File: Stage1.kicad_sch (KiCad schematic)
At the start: 21 parts, among them Q3 SQJQ480E, Q5 IRFR210PBF, U2 LM74800QDRRRQ1

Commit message: new layout
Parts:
- removed D8: 1N4002, Diode_THT:D_DO-41_SOD81_P10.16mm_Horizontal, symbol Diode:1N4002
- added D4: MRA4003T3G, Diode_SMD:D_SMA, symbol Diode:MRA4003T3G
- D6: footprint Diode_THT:D_DO-35_SOD27_P7.62mm_Horizontal -> Diode_SMD:D_SOD-123
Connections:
- net GNDS is gone; now on net GND1: C10.2 (-), C11.2 (-), C2.2 (-), C5.2 (-), C9.2 (-), D2.1 (A1), NT1.1
- net OUT: now also D4.2 (A); no longer C2.1 (+), C5.1 (+), Q3.5 (D), R5.1 (+), U2.12 (C)
- net VS: now also D4.1 (K)
- new net SYSOUT: C2.1 (+), C5.1 (+), Q3.5 (D), R5.1 (+), U2.12 (C)
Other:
- moved on the sheet: NT1
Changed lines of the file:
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@@
+	)
+	(junction
+		(at 99.06 88.9)
+		(diameter 0)
+		(color 0 0 0 0)
 	)
 	(junction
@@
 	)
 	(junction
+		(at 90.17 88.9)
+		(diameter 0)
+		(color 0 0 0 0)
+	)
+	(junction
 		(at 85.09 78.74)
 		(diameter 0)
@@
 	(wire
 		(pts
+			(xy 99.06 90.17) (xy 99.06 88.9)
+		)
+		(stroke
+			(width 0)
+			(type default)
+		)
+	)
+	(wire
+		(pts
 			(xy 132.08 82.55) (xy 132.08 81.28)
 		)
@@
 	(wire
 		(pts
-			(xy 96.52 88.9) (xy 104.14 88.9)
+			(xy 96.52 90.17) (xy 99.06 90.17)
 		)
 		(stroke
@@
 	(wire
 		(pts
+			(xy 90.17 88.9) (xy 99.06 88.9)
+		)
+		(stroke
+			(width 0)
+			(type default)
+		)
+	)
+	(wire
+		(pts
+			(xy 90.17 88.9) (xy 85.09 88.9)
+		)
+		(stroke
+			(width 0)
+			(type default)
+		)
+	)
+	(wire
+		(pts
 			(xy 137.16 118.11) (xy 139.7 118.11)
 		)
@@
 	(wire
 		(pts
+			(xy 99.06 88.9) (xy 104.14 88.9)
+		)
+		(stroke
+			(width 0)
+			(type default)
+		)
+	)
+	(wire
+		(pts
 			(xy 175.26 118.11) (xy 179.07 118.11)
 		)
@@
 	(wire
 		(pts
+			(xy 90.17 90.17) (xy 90.17 88.9)
+		)
+		(stroke
+			(width 0)
+			(type default)
+		)
+	)
+	(wire
+		(pts
 			(xy 146.05 72.39) (xy 146.05 73.66)
 		)
@@
 	(wire
 		(pts
-			(xy 91.44 88.9) (xy 85.09 88.9)
+			(xy 91.44 90.17) (xy 90.17 90.17)
 		)
 		(stroke
@@
 		)
 	)
-	(hierarchical_label "OUT"
+	(hierarchical_label "SYSOUT"
 		(shape output)
 		(at 220.98 62.23 0)
@@
 			)
 		)
-		(property "Footprint" "Diode_THT:D_DO-35_SOD27_P7.62mm_Horizontal"
+		(property "Footprint" "Diode_SMD:D_SOD-123"
 			(at 127.635 77.47 0)
 			(effects
@@
 	)
 	(symbol
-		(lib_id "Diode:1N4002")
-		(at 146.05 77.47 270)
-		(unit 1)
-		(exclude_from_sim no)
-		(in_bom yes)
-		(on_board yes)
-		(dnp no)
-		(fields_autoplaced yes)
-		(property "Reference" "D8"
-			(at 148.59 76.1999 90)
-			(effects
-				(font
-					(size 1.27 1.27)
-				)
-				(justify left)
-			)
-		)
-		(property "Value" "1N4002"
-			(at 148.59 78.7399 90)
-			(effects
-				(font
-					(size 1.27 1.27)
-				)
-				(justify left)
-			)
-		)
-		(property "Footprint" "Diode_THT:D_DO-41_SOD81_P10.16mm_Horizontal"
-			(at 141.605 77.47 0)
-			(effects
-				(font
-					(size 1.27 1.27)
-				)
-				(hide yes)
-			)
-		)
-		(property "Datasheet" "http://www.vishay.com/docs/88503/1n4001.pdf"
-			(at 146.05 77.47 0)
-			(effects
-				(font
-					(size 1.27 1.27)
-				)
-				(hide yes)
-			)
-		)
-		(property "Description" "100V 1A General Purpose Rectifier Diode, DO-41"
-			(at 146.05 77.47 0)
-			(effects
-				(font
-					(size 1.27 1.27)
-				)
-				(hide yes)
-			)
-		)
-		(property "Sim.Device" "D"
-			(at 146.05 77.47 0)
-			(effects
-				(font
-					(size 1.27 1.27)
-				)
-				(hide yes)
-			)
-		)
-		(property "Sim.Pins" "1=K 2=A"
-			(at 146.05 77.47 0)
-			(effects
-				(font
-					(size 1.27 1.27)
-				)
-				(hide yes)
-			)
-		)
-		(pin "2"
-		)
-		(pin "1"
-		)
-		(instances
-			(project "OverVoltageProtection"
-				(path "/3ab01156-4af1-4058-a55c-fa6294991d75/6c85ee69-59dc-40d3-b5ed-3a4bea6d00bc"
-					(reference "D8")
-					(unit 1)
-				)
-			)
-		)
-	)
-	(symbol
 		(lib_id "PCM_Elektuur:C")
 		(at 120.65 77.47 0)
@@
 	(symbol
 		(lib_id "Device:NetTie_2")
-		(at 93.98 88.9 0)
+		(at 93.98 90.17 0)
+		(mirror y)
 		(unit 1)
 		(exclude_from_sim no)
@@
 		(dnp no)
 		(property "Reference" "NT1"
-			(at 93.98 90.678 0)
+			(at 93.98 91.948 0)
 			(effects
 				(font
@@
 		)
 		(property "Value" "NetTie_2"
-			(at 93.98 93.218 0)
+			(at 93.98 94.488 0)
 			(effects
 				(font
@@
 		)
 		(property "Footprint" ""
-			(at 93.98 88.9 0)
+			(at 93.98 90.17 0)
 			(effects
 				(font
@@
 		)
 		(property "Datasheet" "~"
-			(at 93.98 88.9 0)
+			(at 93.98 90.17 0)
 			(effects
 				(font
@@
 		)
 		(property "Description" "Net tie, 2 pins"
-			(at 93.98 88.9 0)
+			(at 93.98 90.17 0)
 			(effects
 				(font
@@
 					(unit 1)
 				)
+			)
+		)
+	)
+	(symbol
+		(lib_id "Diode:MRA4003T3G")
+		(at 146.05 77.47 270)
+		(unit 1)
+		(exclude_from_sim no)
+		(in_bom yes)
+		(on_board yes)
+		(dnp no)
+		(fields_autoplaced yes)
+		(property "Reference" "D4"
+			(at 148.59 76.1999 90)
+			(effects
+				(font
+					(size 1.27 1.27)
+				)
+				(justify left)
+			)
+		)
+		(property "Value" "MRA4003T3G"
+			(at 148.59 78.7399 90)
+			(effects
+				(font
+					(size 1.27 1.27)
+				)
+				(justify left)
+			)
+		)
+		(property "Footprint" "Diode_SMD:D_SMA"
+			(at 141.605 77.47 0)
+			(effects
+				(font
+					(size 1.27 1.27)
+				)
+				(hide yes)
+			)
+		)
+		(property "Datasheet" "http://www.onsemi.com/pub_link/Collateral/MRA4003T3-D.PDF"
+			(at 146.05 77.47 0)
+			(effects
+				(font
+					(size 1.27 1.27)
+				)
+				(hide yes)
+			)
+		)
+		(property "Description" "300V, 1A, General Purpose Rectifier Diode, SMA(DO-214AC)"
+			(at 146.05 77.47 0)
+			(effects
+				(font
+					(size 1.27 1.27)
+				)
+				(hide yes)
+			)
+		)
+		(property "Sim.Device" "D"
+			(at 146.05 77.47 0)
+			(effects
+				(font
+					(size 1.27 1.27)
+				)
+				(hide yes)
+			)
+		)
+		(property "Sim.Pins" "1=K 2=A"
+			(at 146.05 77.47 0)
+			(effects
+				(font
+					(size 1.27 1.27)
+				)
+				(hide yes)
+			)
+		)
+		(pin "1"
+		)
+		(pin "2"
+		)
+		(instances
+			(project ""
+				(path "/3ab01156-4af1-4058-a55c-fa6294991d75/6c85ee69-59dc-40d3-b5ed-3a4bea6d00bc"
+					(reference "D4")
+					(unit 1)
+				)

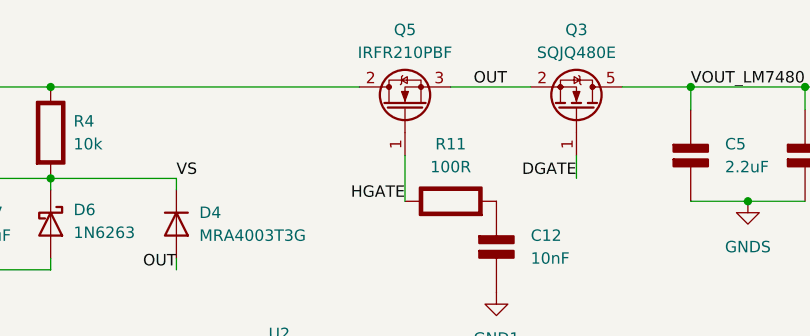
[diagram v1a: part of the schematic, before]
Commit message: change mosfet name
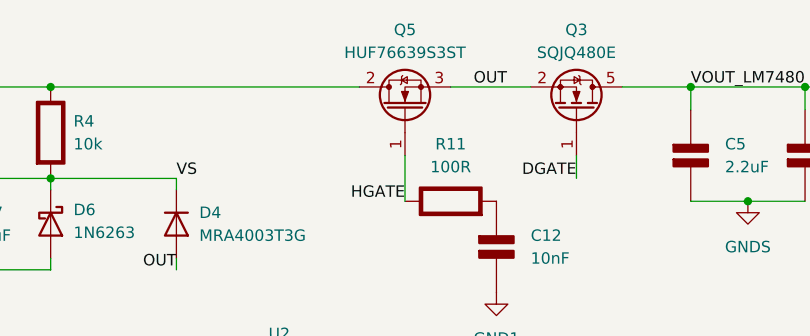
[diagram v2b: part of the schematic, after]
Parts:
- Q5: value IRFR210PBF -> HUF76639S3ST
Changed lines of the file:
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@@
 			)
 		)
-		(property "Value" "IRFR210PBF"
+		(property "Value" "HUF76639S3ST"
 			(at 171.45 58.42 90)
 			(effects

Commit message: fixed HW bug ?
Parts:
- removed Q3: SQJQ480E, Package_TO_SOT_SMD:LFPAK88, symbol Transistor_FET:SQJQ480E
- removed Q5: HUF76639S3ST, Package_TO_SOT_SMD:TO-263-3_TabPin2, symbol Device:Q_NMOS_Depletion_GDS
- added Q7: HUF76639S3ST, Package_TO_SOT_SMD:TO-263-3_TabPin2, symbol Device:Q_NMOS_Depletion_GDS
- added Q8: SQJQ466E-T1_GE3, Package_TO_SOT_SMD:LFPAK88, symbol Transistor_FET:SQJQ480E
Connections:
- net DGATE: now also Q8.1 (G)
- net GND1: no longer C10.2 (-), C11.2 (-), C2.2 (-), C5.2 (-), C9.2 (-), D2.1 (A1), NT1.2
- net HGATE: now also Q7.1 (G)
- net IN: now also Q7.2 (D)
- net OUT: now also Q7.3 (S), Q8.2 (S), Q8.3 (S), Q8.4 (S)
- net SYSOUT: now also Q8.5 (D); no longer R5.1 (+)
- net OV: no longer names the net of R5.2 (-), R6.1 (+), U2.5 (OV)
- new net GNDS: C10.2 (-), C11.2 (-), C2.2 (-), C5.2 (-), C9.2 (-), D2.1 (A1), NT1.2
- new net VOUT: R5.1 (+)
- no-connect marks 0 -> 1
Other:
- moved on the sheet: C2, C5, C8, D2, D4, NT1, R5, R6

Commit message: reworked schematics
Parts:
- C4: footprint Capacitor_SMD:C_0805_2012Metric -> Capacitor_SMD:C_1206_3216Metric
- R4, R5: footprint Resistor_SMD:R_1206_3216Metric_Pad1.30x1.75mm_HandSolder -> Resistor_SMD:R_1206_3216Metric
- R6: value 2.55K -> 2.55k; footprint Resistor_SMD:R_1206_3216Metric_Pad1.30x1.75mm_HandSolder -> Resistor_SMD:R_1206_3216Metric
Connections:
- net VOUT is gone; now on net SYSOUT: R5.1 (+)
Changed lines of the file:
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@@
+		)
+	)
+	(label "VOUT"
+		(at 203.2 62.23 0)
+		(effects
+			(font
+				(size 1.27 1.27)
+			)
+			(justify left bottom)
 		)
 	)
@@
 			)
 		)
-		(property "Footprint" "Resistor_SMD:R_1206_3216Metric_Pad1.30x1.75mm_HandSolder"
+		(property "Footprint" "Resistor_SMD:R_1206_3216Metric"
 			(at 132.08 67.31 0)
 			(effects
@@
 			)
 		)
-		(property "Footprint" "Resistor_SMD:R_1206_3216Metric_Pad1.30x1.75mm_HandSolder"
+		(property "Footprint" "Resistor_SMD:R_1206_3216Metric"
 			(at 124.46 100.33 0)
 			(effects
@@
 			)
 		)
-		(property "Footprint" "Capacitor_SMD:C_0805_2012Metric"
+		(property "Footprint" "Capacitor_SMD:C_1206_3216Metric"
 			(at 184.15 120.65 0)
 			(effects
@@
 			)
 		)
-		(property "Value" "2.55K"
+		(property "Value" "2.55k"
 			(at 127 111.7599 0)
 			(effects
@@
 			)
 		)
-		(property "Footprint" "Resistor_SMD:R_1206_3216Metric_Pad1.30x1.75mm_HandSolder"
+		(property "Footprint" "Resistor_SMD:R_1206_3216Metric"
 			(at 124.46 110.49 0)
 			(effects

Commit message: updated layout
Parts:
- NT1: footprint (none) -> NetTie:NetTie-2_SMD_Pad0.5mm
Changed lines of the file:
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@@
 			)
 		)
-		(property "Footprint" ""
+		(property "Footprint" "NetTie:NetTie-2_SMD_Pad0.5mm"
 			(at 93.98 88.9 0)
 			(effects
